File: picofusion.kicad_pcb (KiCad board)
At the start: 4 copper layers, 25.5 x 25.5 mm, 69 parts, among them J1 NORTH, J2 EAST, J3 WEST, J4 SOUTH, U1 W25Q16, U2 RP2040, U3 TLV71333PDQN, U4 ICM-20602, U5 MMC5983MA, U6 ICP20100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

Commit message: R02B: more work
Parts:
- moved R20 5.59 mm to (162.3, 34.6), turned to -90 degrees
- moved R19 3.74 mm to (163.3, 34.6), turned to -90 degrees
- moved D1 3.47 mm to (164.8, 31.7), turned to -90 degrees
- moved R6 1.49 mm to (168.8, 34.1), turned to 0 degrees
- moved R1 1.42 mm to (157.6, 31.2)
- moved D2 1.03 mm to (166.9, 34.1)
- moved C16 0.83 mm to (168.1, 32.7)
- moved D3 0.81 mm to (166.3, 31.7)
- moved U3 0.62 mm to (167.9, 31.2)
- moved U6 0.50 mm to (159.8, 32.6)
- moved C14 0.46 mm to (169.2, 31.2)
- moved C23 0.45 mm to (159.8, 30.7)
- moved C22 0.45 mm to (161.8, 32.6)
- moved R2 0.40 mm to (165.0, 35.6)
- moved R3 0.40 mm to (166.1, 35.6)
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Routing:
- net /QSPI_nCS: track 17.9 -> 12.4 mm, vias 2 -> 0
- net GND: track 40.4 -> 45.3 mm, vias 43 -> 42
- net /RUN: track 32.9 -> 30.6 mm, vias 1 -> 2
- net /I2C0_SCL: track 32.9 -> 35.2 mm
- net +5V: track 34.5 -> 36.8 mm, vias 4 -> 3
- net /BOOTSEL: track 6.35 -> 8.17 mm, vias 0 -> 1
- net /USB_DN: track 7.91 -> 9.46 mm, vias 1 -> 0
- net /USB_DP: track 7.96 -> 9.46 mm, vias 1 -> 0
- net /SWDIO: track 24.3 -> 25.8 mm
- net /SWCLK: track 34.1 -> 33.1 mm
- net +3V3: track 43.1 -> 43.8 mm, vias 26 -> 27
- net /USB_MCU_DP: track 4.33 -> 3.69 mm

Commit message: R02B: finish new discussion modifications
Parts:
- removed C29: 0.1uF, Capacitor_SMD:C_0402_1005Metric
- removed R14, R15, R16, R17, R22, R24: 0, Resistor_SMD:R_0402_1005Metric
- added G***: LOGO, LOGO, F.Cu at (154.9, 50.5)
- C1, C10, C11, C12, C13, C15, C17, C18, C19, C2, C21, C22, C23, C24, C25, C26, C27, C28, C3, C4, C6, C7, C9: footprint Capacitor_SMD:C_0402_1005Metric -> Capacitor_SMD:C_0201_0603Metric
- C14, C16: footprint Capacitor_SMD:C_0402_1005Metric -> Capacitor_SMD:C_0603_1608Metric
- J1, J2, J3, J4: footprint picofusion_stamp:Castellated_1x8_P2.54mm_Vertical -> Connector_PinHeader_2.00mm:PinHeader_1x10_P2.00mm_Vertical
- R1, R2, R20, R3, R8, R9: footprint Resistor_SMD:R_0402_1005Metric -> Resistor_SMD:R_0201_0603Metric
- U4: value ICM-20602 -> ICM42605; footprint Package_LGA:LGA-16_3x3mm_P0.5mm_LayoutBorder3x5y -> Package_LGA:LGA-14_3x2.5mm_P0.5mm_LayoutBorder3x4y
- moved C11 19.4 mm to (168.8, 46.2)
- moved R1 19.2 mm to (169.6, 46.2)
- moved R19 16.9 mm to (170.3, 50.0)
- moved R20 15.4 mm to (169.8, 48.1), turned to 180 degrees
- moved R21 15.1 mm to (169.3, 50.0)
- moved J1 9.03 mm to (151.0, 27.2)
- moved J2 9.03 mm to (172.8, 31.0)
- moved J3 9.03 mm to (147.2, 31.0)
- moved J4 9.03 mm to (151.0, 52.8)
- moved R23 7.84 mm to (150.1, 37.3)
- moved R7 5.54 mm to (151.2, 37.3), turned to -90 degrees
- moved C19 4.24 mm to (152.8, 40.3), turned to 180 degrees
- moved R4 4.14 mm to (170.1, 41.8), turned to 0 degrees
- moved R18 4.04 mm to (170.6, 46.3)
- moved C15 2.01 mm to (169.1, 44.0), turned to 0 degrees
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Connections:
- J1 pad 1: /SWCLK -> unconnected-(J1-Pad1)
- J1 pad 2: /SWDIO -> unconnected-(J1-Pad2)
- J1 pad 3: /RUN -> unconnected-(J1-Pad3)
- J1 pad 4: /BOOTSEL -> unconnected-(J1-Pad4)
- J1 pad 5: /USB_DP -> GND
- J1 pad 6: /USB_DN -> /USB_DP
- J1 pad 7: +5V -> /USB_DN
- J1 pad 8: GND -> +5V
- J2 pad 6: /UART1_RX_GNSS -> GND
- J2 pad 7: /UART1_TX_GNSS -> /UART1_RX_GNSS
- J2 pad 8: GND -> /UART1_TX_GNSS
- J3 pad 1: /SDA/SDI -> /SPI0_nCS
- J3 pad 2: /SCL/SCK -> /SPI0_SCK
- J3 pad 3: /SPI0_POCI -> /SPI0_PICO
- J3 pad 4: /NEOPIXEL -> /SPI0_POCI
- J3 pad 5: +3V3 -> /DRDY_ICM42605
- J3 pad 6: /CAN_N -> +3V3
- J3 pad 7: /CAN_P -> /CAN_N
- J3 pad 8: GND -> /CAN_P
- J4 pad 1: +5V -> /LED
- U2 pad 8: /DRDY_ICM20602 -> /DRDY_ICM42605
- U2 pad 9: /NEOPIXEL -> /LED
- U4 pad 1: +3V3 -> /SPI0_POCI
- U4 pad 10: GND -> unconnected-(U4-Pad10)
- U4 pad 11: GND -> unconnected-(U4-Pad11)
- U4 pad 12: GND -> /SPI0_nCS
- U4 pad 13: GND -> /SPI0_SCK
- U4 pad 14: Net-(C29-Pad1) -> /SPI0_PICO
- U4 pad 2: /SPI0_SCK -> unconnected-(U4-Pad2)
- U4 pad 3: /SPI0_PICO -> unconnected-(U4-Pad3)
- U4 pad 4: /SPI0_POCI -> /DRDY_ICM42605
- U4 pad 5: /SPI0_nCS -> +3V3
- U4 pad 6: /DRDY_ICM20602 -> GND
- U4 pad 8: GND -> +3V3
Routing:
- net /SWCLK: track 33.1 -> 6.95 mm
- net /NEOPIXEL: track 20.7 -> 0.00 mm, vias 2 -> 0
- net /LED: track 0.00 -> 17.5 mm, vias 0 -> 1
- net /RUN: track 30.6 -> 13.4 mm, vias 2 -> 1
- net GND: track 45.3 -> 28.4 mm, vias 42 -> 47
- net /DRDY_ICM42605: track 0.00 -> 16.8 mm
- net /SWDIO: track 25.8 -> 9.71 mm
- net /DRDY_ICM20602: track 13.3 -> 0.00 mm, vias 2 -> 0
- net +3V3: track 43.8 -> 31.5 mm
- net /SDA/SDI: track 10.4 -> 0.00 mm, vias 2 -> 0
- net /SCL/SCK: track 10.4 -> 0.00 mm, vias 1 -> 0
- net /QSPI_nCS: track 12.4 -> 22.2 mm, vias 0 -> 2
- net /I2C0_SCL: track 35.2 -> 26.3 mm, vias 3 -> 2
- net /SPI0_SCK: track 13.3 -> 19.8 mm, vias 3 -> 2
- net /SPI0_nCS: track 29.4 -> 23.8 mm
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- added copper zone on F.Cu, net +3V3

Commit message: more board cleanup, silkscreen draft
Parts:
- removed the G*** at (154.9, 50.5)
- added G***: LOGO, LOGO, F.Cu at (155.4, 29.4)
- added G***: LOGO, LOGO, F.Cu at (157.0, 50.8)
- J1, J2, J3, J4: footprint Connector_PinHeader_2.00mm:PinHeader_1x10_P2.00mm_Vertical -> picofusion_stamp:PinCastellation_1x10_P2.00mm_Vertical
- U4: footprint Package_LGA:LGA-14_3x2.5mm_P0.5mm_LayoutBorder3x4y -> ICM-42605:PQFN50P300X250X97-14N
- moved C27 0.10 mm to (151.4, 42.8)
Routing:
- net /UART0_TX_TELEM: track 13.8 -> 14.7 mm
- net GND: track 28.4 -> 27.9 mm, vias 47 -> 46

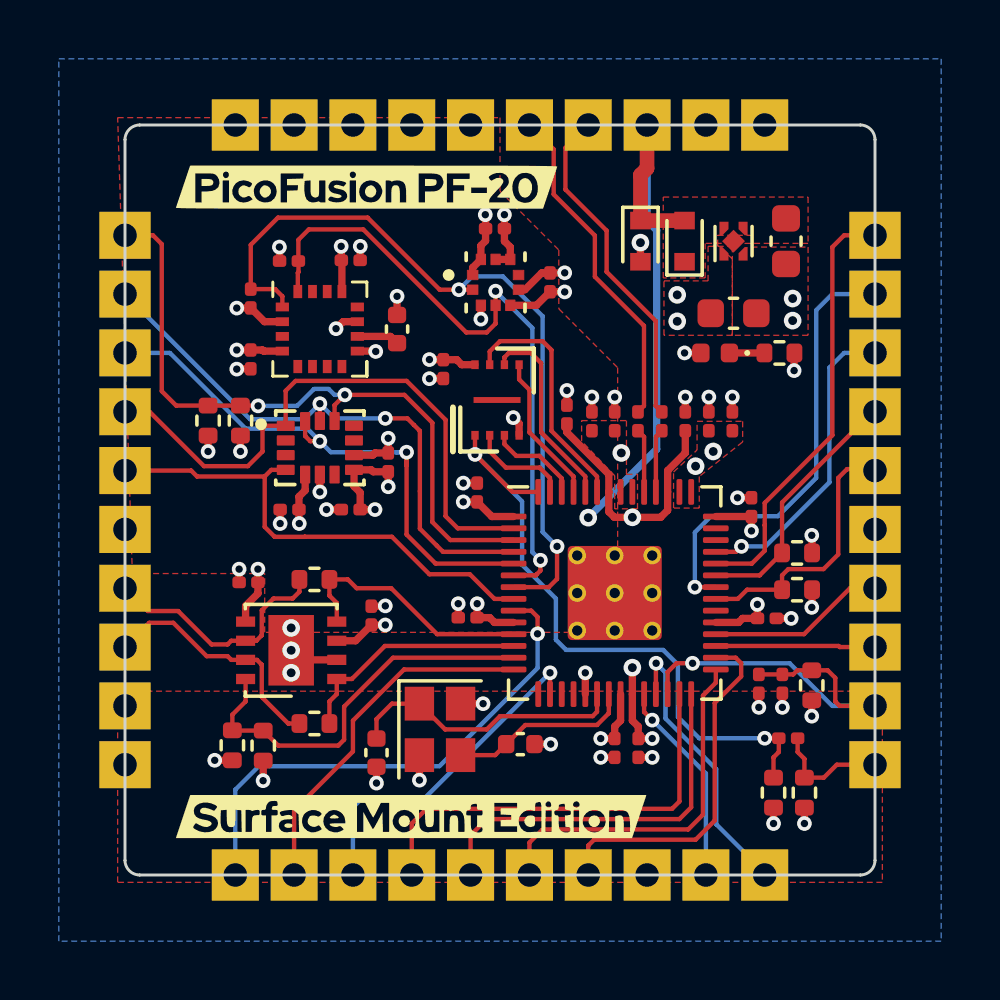
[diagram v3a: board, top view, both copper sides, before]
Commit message: update footprints, fix drc
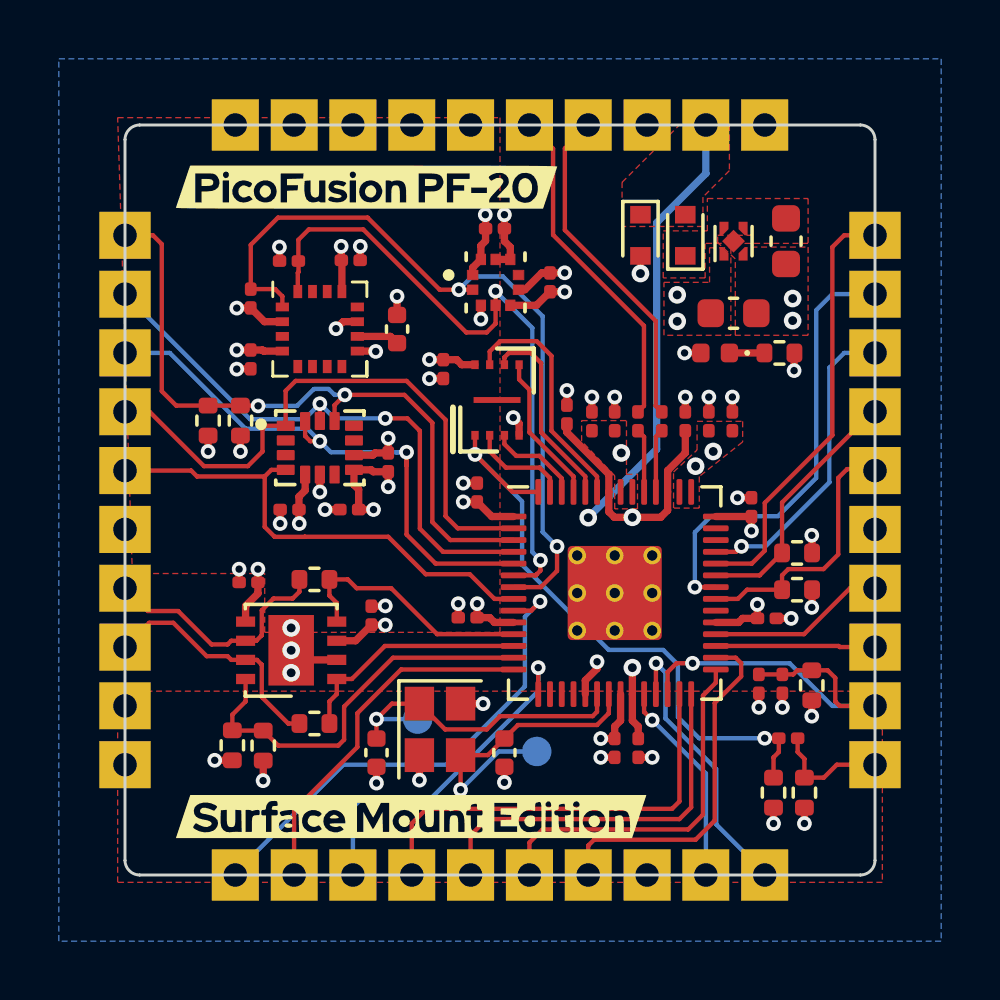
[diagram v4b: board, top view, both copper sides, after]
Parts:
- added TP1: TestPoint, TestPoint:TestPoint_Pad_D1.0mm, B.Cu at (157.2, 47.5)
- added TP2: TestPoint, TestPoint:TestPoint_Pad_D1.0mm, B.Cu at (161.2, 48.5)
- C5, C8: value 12pF -> 10pF
- moved D1 1.54 mm to (166.3, 31.0), turned to 90 degrees
- moved D3 1.51 mm to (164.8, 31.0), turned to -90 degrees
- moved C8 0.61 mm to (160.2, 48.6), turned to -90 degrees
- moved C17 0.05 mm to (154.9, 40.3)
- renumbered J2 to Je
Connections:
- D1 pad 1: +5V -> Net-(C14-Pad1)
- D1 pad 2: GND -> +5V
- D3 pad 1: Net-(C14-Pad1) -> +5V
- D3 pad 2: +5V -> GND
- J1 pad 10: unconnected-(J1-Pad10) -> GND
- J1 pad 5: GND -> unconnected-(J1-Pad5)
- J1 pad 8: +5V -> GND
- J1 pad 9: GND -> +5V
- U2 pad 15: unconnected-(U2-Pad15) -> /BUZZER
- U2 pad 16: /BUZZER -> unconnected-(U2-Pad16)
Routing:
- net /XOUT: track 6.28 -> 10.6 mm, vias 0 -> 1
- net +5V: track 39.9 -> 35.9 mm
- net /XIN: track 9.59 -> 11.0 mm, vias 0 -> 1
- net /LED: track 17.5 -> 16.6 mm
- net +1V1: track 16.8 -> 16.3 mm, vias 3 -> 2
- added copper zone on F.Cu, net +5V
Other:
- board text removed: "Designed by: Kalyan Sriram Kush Nayak Vincent Wang"

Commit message: h10: add graphics, fix drc, minor modifications
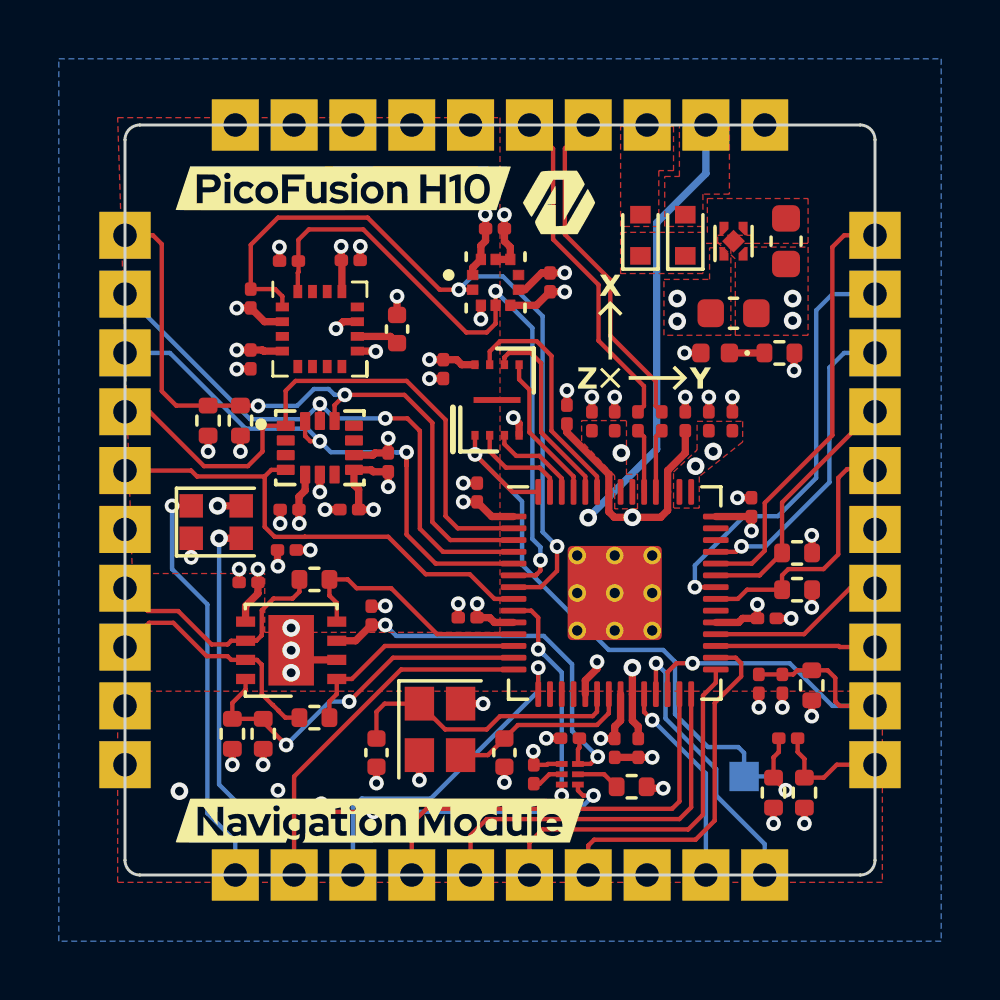
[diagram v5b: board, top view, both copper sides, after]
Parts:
- removed the G*** at (155.4, 29.4)
- removed the G*** at (157.0, 50.8)
- removed TP2: TestPoint, TestPoint:TestPoint_Pad_D1.0mm
- added C29: 0.1uF, Capacitor_SMD:C_0201_0603Metric, F.Cu at (161.2, 49.3)
- added C30: 0.1uF, Capacitor_SMD:C_0201_0603Metric, F.Cu at (162.4, 48.1)
- added C31: 1uF, Capacitor_SMD:C_0201_0603Metric, F.Cu at (152.8, 41.7)
- added D4: WS2812B-2020, LED_SMD_Extra:WS2812B-2020, F.Cu at (150.3, 40.8)
- added G***: LOGO, picofusion_stamp:compass, F.Cu at (165.0, 34.6)
- added G***: LOGO, LOGO, B.Cu at (169.8, 41.0)
- added G***: LOGO, LOGO, B.Cu at (161.0, 50.2)
- added G***: LOGO, LOGO, B.Cu at (163.0, 30.3)
- added G***: LOGO, picofusion_stamp:hobby-edition, B.Cu at (158.6, 36.8)
- added G***: LOGO, LOGO, B.Cu at (150.4, 43.0)
- added G***: LOGO, LOGO, B.Cu at (169.7, 43.0)
- added G***: LOGO, picofusion_stamp:picofusion-h10-large, B.Cu at (160.0, 33.6)
- added G***: LOGO, LOGO, B.Cu at (161.0, 30.4)
- added G***: LOGO, picofusion_stamp:ahrs, B.Cu at (161.0, 35.5)
- added G***: LOGO, LOGO, B.Cu at (150.5, 45.0)
- added G***: LOGO, picofusion_stamp:picofusion-h10, F.Cu at (154.7, 29.4)
- added G***: LOGO, LOGO, B.Cu at (159.0, 50.9)
- added G***: LOGO, LOGO, B.Cu at (167.0, 30.2)
- added G***: LOGO, LOGO, B.Cu at (150.2, 41.0)
- added G***: LOGO, LOGO, B.Cu at (169.0, 30.2)
- added G***: LOGO, LOGO, B.Cu at (165.0, 30.2)
- added G***: LOGO, LOGO, B.Cu at (163.0, 50.3)
- added G***: LOGO, LOGO, B.Cu at (169.7, 45.0)
- added G***: LOGO, LOGO, B.Cu at (157.0, 50.9)
- added G***: LOGO, LOGO, F.Cu at (162.0, 29.9)
- added G***: LOGO, picofusion_stamp:navigation-module, F.Cu at (155.9, 50.9)
- added G***: LOGO, LOGO, B.Cu at (153.0, 50.2)
- added G***: LOGO, LOGO, B.Cu at (150.3, 49.0)
- added G***: LOGO, LOGO, B.Cu at (165.0, 49.8)
- added G***: LOGO, LOGO, B.Cu at (169.7, 47.0)
- added G***: LOGO, LOGO, B.Cu at (150.2, 47.0)
- added R14: 10K, Resistor_SMD:R_0402_1005Metric, F.Cu at (164.5, 49.8)
- added U8: 74LVC1T45GS, 74LVC1T45:PSON35P100X100X35-6N, F.Cu at (162.4, 49.3)
- TP1: footprint TestPoint:TestPoint_Pad_D1.0mm -> TestPoint:TestPoint_Pad_1.0x1.0mm
- moved TP1 11.3 mm to (168.3, 49.4)
- moved G*** 8.42 mm to (157.0, 44.7)
- moved R11 0.40 mm to (151.9, 48.0)
- moved R10 0.39 mm to (150.9, 48.0)
- moved R12 0.20 mm to (153.7, 47.4)
- turned D3 to 90 degrees
- renumbered Je to J2
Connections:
- C14 pad 1: Net-(C14-Pad1) -> /5V_RECT
- D1 pad 1: Net-(C14-Pad1) -> /5V_RECT
- D3 pad 1: +5V -> /5V_RECT
- J3 pad 10: +5V -> +3V3
- J3 pad 6: +3V3 -> +5V
- TP1 pad 1: /XIN -> /QSPI_nCS
- U2 pad 9: /LED -> /LED_3V3
- U3 pad 3: Net-(C14-Pad1) -> /5V_RECT
- U3 pad 4: Net-(C14-Pad1) -> /5V_RECT
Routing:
- net /NEOPIXEL: track 0.00 -> 23.3 mm, vias 0 -> 4
- net +5V: track 35.9 -> 49.3 mm, vias 2 -> 5
- net /LED_3V3: track 0.00 -> 7.70 mm, vias 0 -> 2
- net /XOUT: track 10.6 -> 6.28 mm, vias 1 -> 0
- net /LED: track 16.6 -> 14.0 mm
- net GND: track 28.4 -> 30.7 mm, vias 46 -> 49
- net /QSPI_nCS: track 21.7 -> 23.7 mm
- net +3V3: track 31.5 -> 33.4 mm, vias 27 -> 29
- net Net-(R14-Pad2): track 0.00 -> 1.49 mm
- net /XIN: track 11.0 -> 9.73 mm, vias 1 -> 0
- net /CAN_SILENT: track 13.6 -> 12.8 mm, vias 0 -> 2
- net /SPI1_POCI_SD: track 15.3 -> 14.7 mm
- added copper zone on F.Cu, net /5V_RECT
- removed copper zone on F.Cu, net Net-(C14-Pad1)
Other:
- board text removed: "JLCJLCJLCJLC"
- board text removed: "MOD-PICOFUSION-R01B"
- board text removed: "PicoFusion AHRS"

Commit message: h10: r2 final
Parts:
- added G***: LOGO, picofusion_stamp:rev, B.Cu at (162.6, 38.1)
- added G***: LOGO, picofusion_stamp:r2, F.Cu at (170.5, 29.2)
- added R15: 22K, Resistor_SMD:R_0201_0603Metric, F.Cu at (167.9, 29.2)
- added R16: 22K, Resistor_SMD:R_0201_0603Metric, F.Cu at (169.4, 29.2)
- added R17: 22K, Resistor_SMD:R_0201_0603Metric, F.Cu at (169.5, 36.5)
- added R22: 22K, Resistor_SMD:R_0201_0603Metric, F.Cu at (169.5, 37.3)
- R2, R3: value 27.4 -> 27
- moved G*** 11.9 mm to (150.2, 31.5)
- moved G*** 0.50 mm to (150.0, 45.0)
- moved G*** 0.40 mm to (150.0, 43.0)
- moved G*** 0.20 mm to (154.7, 29.2)
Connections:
- J1 pad 3: unconnected-(J1-Pad3) -> /RESV1
- J1 pad 4: unconnected-(J1-Pad4) -> /I2C0_SCL
- J1 pad 5: unconnected-(J1-Pad5) -> /I2C0_SDA
- U2 pad 16: unconnected-(U2-Pad16) -> /RESV1
- U2 pad 40: unconnected-(U2-Pad40) -> /3V3_SENSE
- U2 pad 41: unconnected-(U2-Pad41) -> /5V_SENSE
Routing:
- net /RESV1: track 0.00 -> 23.2 mm, vias 0 -> 1
- net /5V_SENSE: track 0.00 -> 16.9 mm
- net /I2C0_SDA: track 22.4 -> 30.6 mm
- net /3V3_SENSE: track 0.00 -> 7.67 mm, vias 0 -> 2
- net /I2C0_SCL: track 26.2 -> 32.3 mm, vias 2 -> 3
- net GND: track 30.7 -> 32.1 mm, vias 49 -> 53
- net /QSPI_nCS: track 23.7 -> 23.1 mm
- net +3V3: track 33.4 -> 33.9 mm, vias 29 -> 30
